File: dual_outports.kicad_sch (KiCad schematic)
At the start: 25 parts, among them J301 USB_A, J302 USB_A, SW301 SW_Push, SW302 SW_Push, U201 USBLC6-2P6, U203 USBLC6-2P6, U302 MIC2026-1xM, U304 74LVC2G08

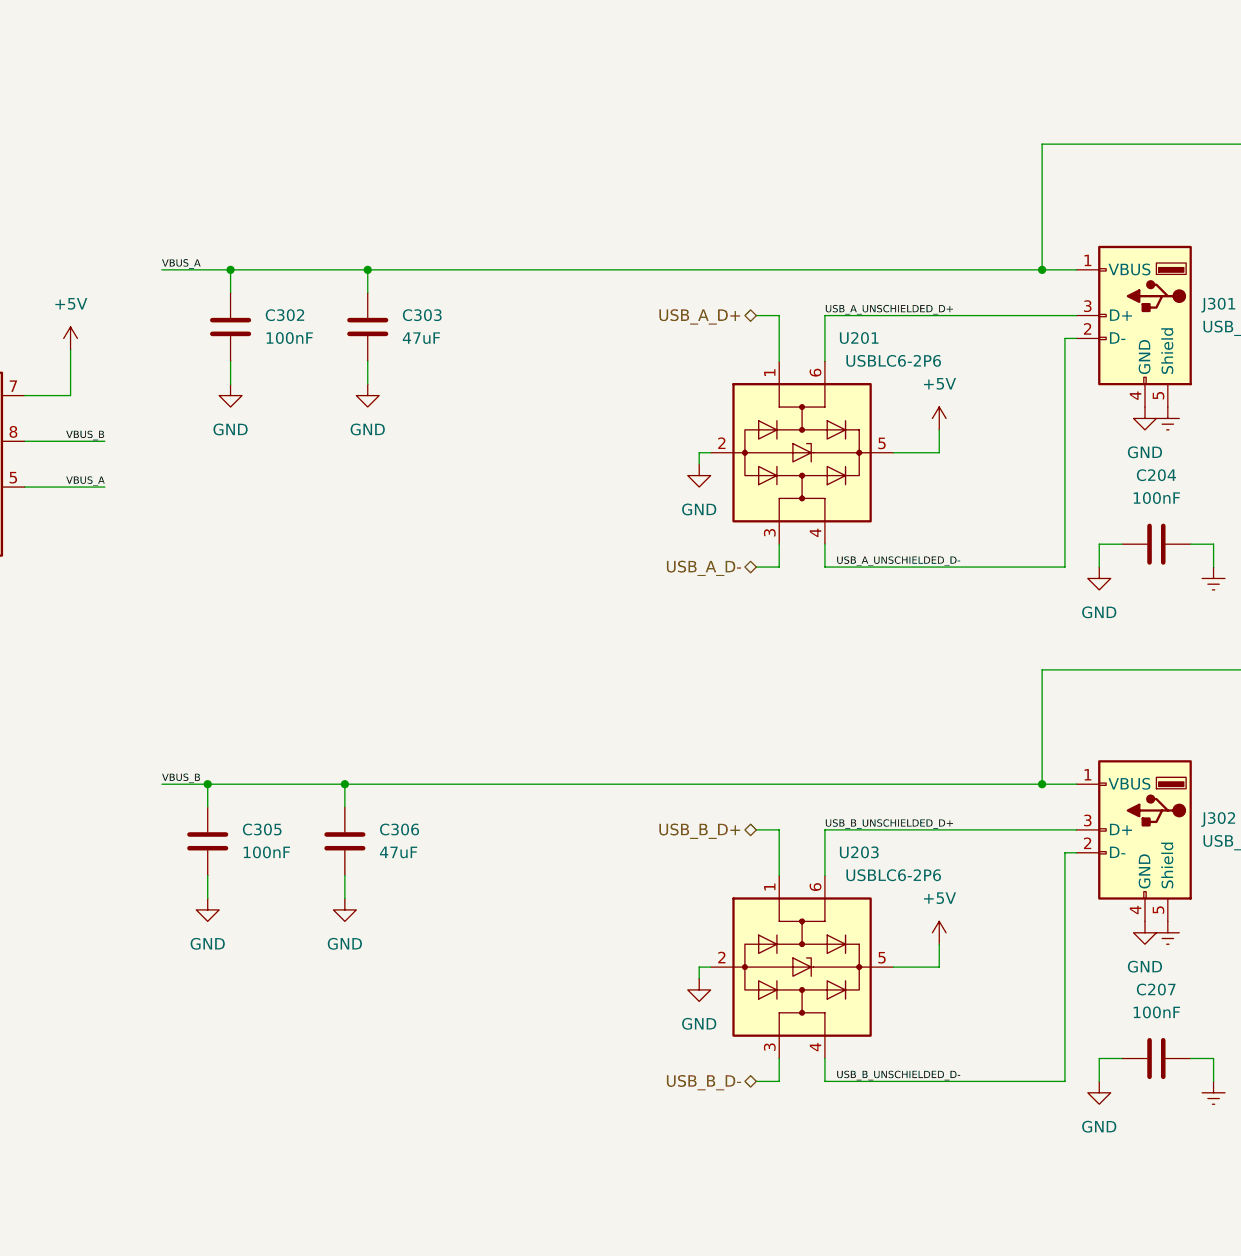
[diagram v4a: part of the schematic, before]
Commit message: Update to new enviroment
Kicad 8 & global symbols and footprint library
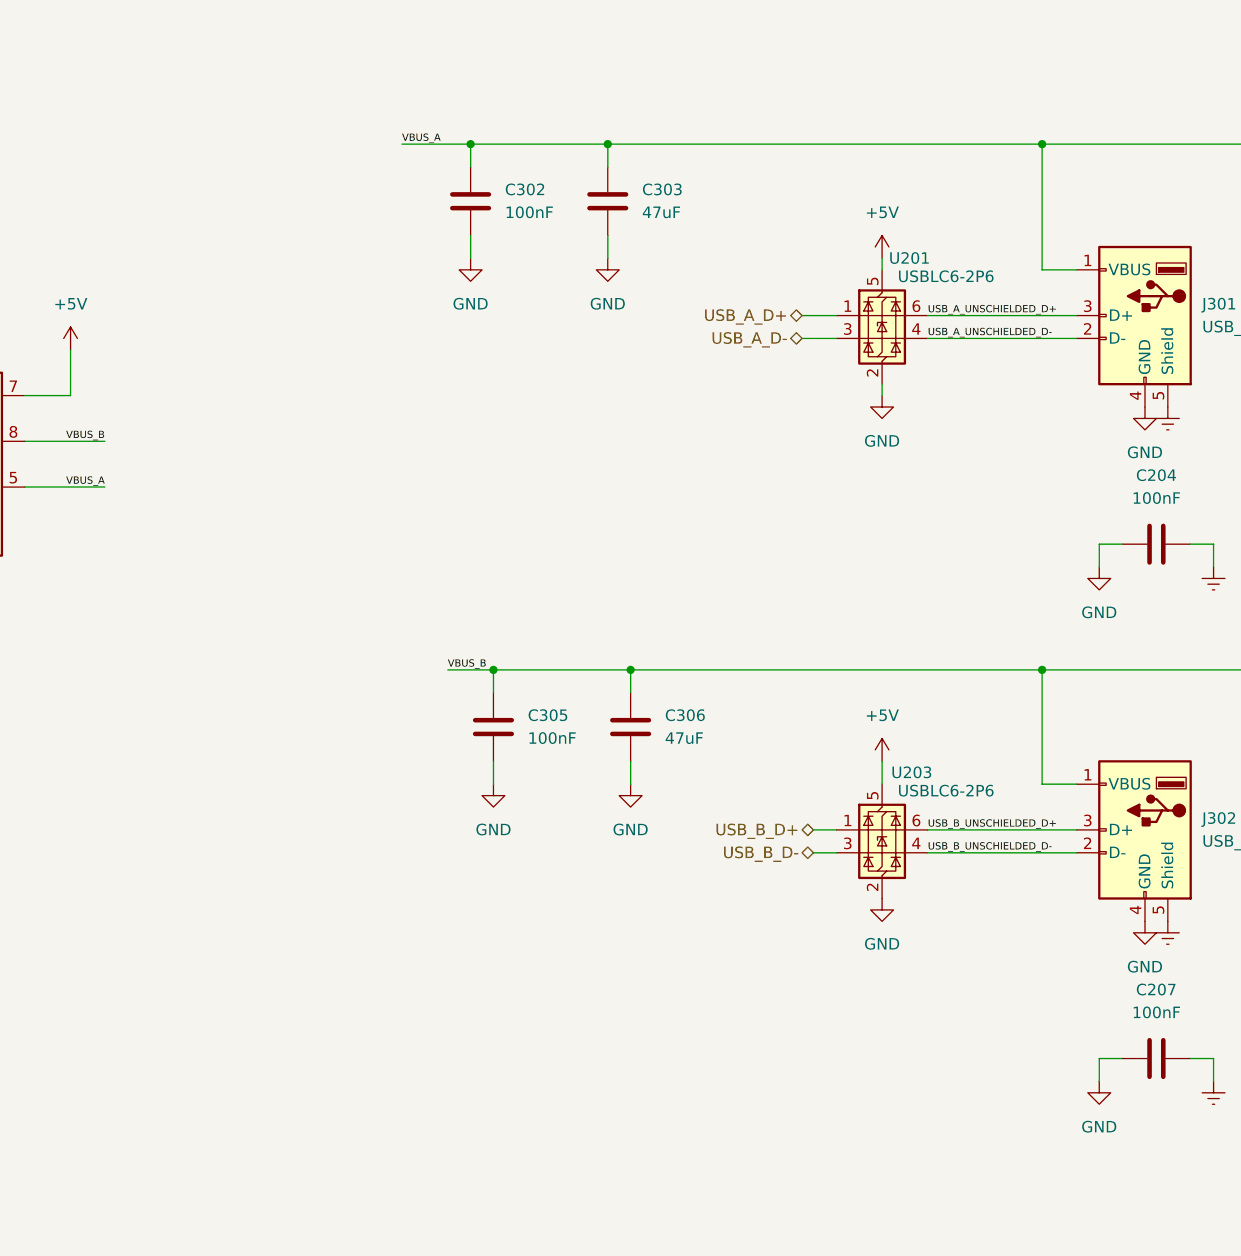
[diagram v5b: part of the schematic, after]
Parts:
- J301, J302: footprint Connectors:UJ2-AV-W4-TH -> g-Connector_USB:UJ2-AV-W4-TH
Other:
- moved on the sheet: C302, C303, C305, C306
